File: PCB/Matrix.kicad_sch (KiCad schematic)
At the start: 133 parts, among them SW1 MX, SW10 MX, SW11 MX, SW12 MX, SW13 MX, SW14 MX, SW15 MX, SW16 MX, SW17 MX, SW18 MX, SW19 MX, SW2 MX, SW20 MX, SW21 MX, SW22 MX, SW23 MX, SW24 MX, SW25 MX, SW26 MX, SW27 MX, SW28 MX, SW29 MX, SW3 MX, SW30 MX, SW31 MX, SW32 MX, SW33 MX, SW34 MX, SW35 MX, SW36 MX, SW37 MX, SW38 MX, SW39 MX, SW4 MX, SW40 MX, SW41 MX, SW42 MX, SW43 MX, SW44 MX, SW45 MX, SW46 MX, SW47 MX, SW48 MX, SW49 MX, SW5 MX, SW50 MX, SW51 MX, SW52 MX, SW53 MX, SW54 MX, SW55 MX, SW56 MX, SW57 MX, SW58 MX, SW59 MX, SW6 MX, SW60 MX, SW61 MX, SW62 MX, SW63 MX, SW64 Encoder, SW7 MX, SW8 MX, SW9 MX

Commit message: Massive mistake corrections and clarifications.
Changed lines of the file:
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@@
-    (stroke (width 0) (type default))
-  )
-  (wire (pts (xy 259.08 74.93) (xy 261.62 74.93))
     (stroke (width 0) (type default))
   )
@@
     (stroke (width 0) (type default))
   )
-  (wire (pts (xy 259.08 74.93) (xy 259.08 72.39))
+  (wire (pts (xy 259.08 72.39) (xy 259.08 74.93))
     (stroke (width 0) (type default))
   )
@@
     (stroke (width 0) (type default))
   )
-  (wire (pts (xy 251.46 52.07) (xy 251.46 67.31))
-    (stroke (width 0) (type default))
-  )
   (wire (pts (xy 87.63 88.9) (xy 87.63 86.36))
     (stroke (width 0) (type default))
@@
     (stroke (width 0) (type default))
   )
+  (wire (pts (xy 248.92 52.07) (xy 248.92 54.61))
+    (stroke (width 0) (type default))
+  )
   (wire (pts (xy 133.35 40.64) (xy 133.35 55.88))
     (stroke (width 0) (type default))
@@
     (stroke (width 0) (type default))
   )
+  (wire (pts (xy 256.54 49.53) (xy 256.54 52.07))
+    (stroke (width 0) (type default))
+  )
   (wire (pts (xy 158.75 71.12) (xy 158.75 86.36))
     (stroke (width 0) (type default))
@@
     (stroke (width 0) (type default))
   )
-  (wire (pts (xy 248.92 52.07) (xy 251.46 52.07))
-    (stroke (width 0) (type default))
-  )
   (wire (pts (xy 52.07 55.88) (xy 52.07 71.12))
     (stroke (width 0) (type default))
@@
     (stroke (width 0) (type default))
   )
+  (wire (pts (xy 251.46 67.31) (xy 251.46 49.53))
+    (stroke (width 0) (type default))
+  )
   (wire (pts (xy 54.61 71.12) (xy 52.07 71.12))
     (stroke (width 0) (type default))
@@
     (stroke (width 0) (type default))
   )
+  (wire (pts (xy 251.46 49.53) (xy 256.54 49.53))
+    (stroke (width 0) (type default))
+  )
   (wire (pts (xy 123.19 40.64) (xy 123.19 43.18))
     (stroke (width 0) (type default))
@@
     (stroke (width 0) (type default))
   )
-  (wire (pts (xy 243.84 74.93) (xy 241.3 74.93))
-    (stroke (width 0) (type default))
-  )
   (wire (pts (xy 110.49 43.18) (xy 110.49 40.64))
     (stroke (width 0) (type default))
@@
     (stroke (width 0) (type default))
   )
-  (wire (pts (xy 248.92 54.61) (xy 246.38 54.61))
-    (stroke (width 0) (type default))
-  )
   (wire (pts (xy 87.63 86.36) (xy 85.09 86.36))
     (stroke (width 0) (type default))
@@
   (wire (pts (xy 215.9 86.36) (xy 213.36 86.36))
     (stroke (width 0) (type default))
-  )
-  (image (at 205.74 173.99) (scale 1.29633)
-    (data
-      iVBORw0KGgoAAAANSUhEUgAAAgAAAACACAYAAAB9V9ELAAAABHNCSVQICAgIfAhkiAAABRFJREFU
-      eJzt3Uty3DgQBUDZMfe/smdpDz0hCsKvgJe5tdxkg6RUgVcAPz4AAAAAAAAAgBv82H0ClPer8efd
-      UwAH+Ln7BACA9RQAABBIAQAAgeS1PD0z/7d75K1HwD0GUJAZAAAIpAAAgEAKAAAI9M/uE2C51nX9
-      b54Z/+jPB37Tc8MwZgAAIJACAAACKQAAIJAegPv1Zoat+wIA47T21Hhe+TIzAAAQSAEAAIEUAAAQ
-      SA/AfawThnPZR4NlzAAAQCAFAAAEUgAAQCA9AOdpzQhl/nAP795gGDMAABBIAQAAgRQAABBID0B9
-      1vUDMJwZAAAIpAAAgEAKAAAIpAegntGZf+v7wa0rBghgBgAAAikAACCQAgAAAukB2G925v/272+f
-      f/s+A/ZZACKZAQCAQAoAAAikAACAQHoA5mtdV9+bOa9+X7h9AwAOZAYAAAIpAAAgkAIAAALpARiv
-      2rpy69g/Z3yASGYAACCQAgAAAikAACCQHoB+1TL/VqPX8Vf/vgB8mAEAgEgKAAAIpAAAgEB6AN6t
-      3su/9fijj7c6w9/dQ7H7+NDCuzcYxgwAAARSAABAIAUAAATSA/C33Znw7Iyv9/N3Z5C7jz9a7/c5
-      vedk9/Htg9Hm9vuj9/OrPc+fMgMAAIEUAAAQSAEAAIFuz6u+Ynem9bQ642r9vNHnVz3Tn50pjrZ6
-      /HePT/X77bTr8bT7fG6/P1oNvb5mAAAgkAIAAAIpAAAgUGIPwOwMu9qYzl7XelrG13r8ahnu6HdT
-      rF4Hf9rxVl+P1Z/fe7xWq++Pascfret6mwEAgEAKAAAIpAAAgEA3vgugWia32u69rGc7rcfiTev3
-      ef58tetV7Xxa3XY93qzuKdndkzG7Z+uovydmAAAgkAIAAAIpAAAg0A09ANX38q/+fuzTMsvTVeth
-      SFd93fxuvT0RT7N/X6/uyRh9vk9TexrMAABAIAUAAARSAABAoBN7AHZn/rvX/d6Wod3utsx/9P0x
-      +vNm369pz8PonqbdPVH8wQwAAARSAABAIAUAAAQ6oQegNfNevQ5/d6bVu/d09Yy62vnt7kGppjXD
-      rz4+ozPk2XvDr+75qfb7Y/d4zTa1J8sMAAAEUgAAQCAFAAAEqtADMDvDqZZZvZmd+dMmffyuyjz/
-      x+z305/mtn1Abrs+Q5kBAIBACgAACKQAAIBAO3oATl8n3Gv2908f391m95ycnsmeLu16vvUErO6x
-      qj5eRzEDAACBFAAAEEgBAACBVvQApGXSq/c1GP35b/9/dwbI54x/n9PGr9rzN/p8ZP5tmsbfDAAA
-      BFIAAEAgBQAABBrRA1At46+2DnV1BrY7AzzN7L3PezNRGehcq5+X6tdz9/2/+/hRzAAAQCAFAAAE
-      UgAAQKDv9AC0ZjSnZTC7M/dqPRWt3q539Qx0ttXvt69+v/TqHc/Rz9vo69v6/FR//nqP39tDsPv7
-      l2IGAAACKQAAIJACAAACfSXf6s3ITs9cdu8rUD3DnX19q6/Tdv//V/VMvZrq47F7L//Tjz9b1/Nm
-      BgAAAikAACCQAgAAAq3oAUi3e1+B1W7L3Kpn2qPXec/OXKu9G+P0Hpbd17vV7r8nu48/mh4AAKCN
-      AgAAAikAACDQd/KOtEz76bTMDQD+YgYAAAIpAAAgkAIAAAKNyKNPz8Rnr8sGgHLMAABAIAUAAARS
-      AABAoBV59env85bpA3AdMwAAEEgBAACBFAAAAAAAAAAAAABwqH8BSZ/NA/X8f8AAAAAASUVORK5C
-      YII=
-    )
   )
   (hierarchical_label "COL6" (shape input) (at 120.65 22.86 90) (fields_autoplaced)
@@
     (effects (font (size 1.27 1.27)) (justify left))
   )
-  (hierarchical_label "GND" (shape output) (at 261.62 74.93 0) (fields_autoplaced)
-    (effects (font (size 1.27 1.27)) (justify left))
-  )
   (hierarchical_label "COL2" (shape input) (at 52.07 22.86 90) (fields_autoplaced)
     (effects (font (size 1.27 1.27)) (justify left))
   )
-  (hierarchical_label "GND" (shape output) (at 241.3 74.93 180) (fields_autoplaced)
-    (effects (font (size 1.27 1.27)) (justify right))
-  )
   (hierarchical_label "COL9" (shape input) (at 158.75 22.86 90) (fields_autoplaced)
     (effects (font (size 1.27 1.27)) (justify left))
   )
-  (hierarchical_label "GND" (shape output) (at 248.92 52.07 180) (fields_autoplaced)
-    (effects (font (size 1.27 1.27)) (justify right))
-  )
   (hierarchical_label "ROW0" (shape output) (at 186.69 35.56 0) (fields_autoplaced)
     (effects (font (size 1.27 1.27)) (justify left))
@@
   (hierarchical_label "COL5" (shape input) (at 90.17 22.86 90) (fields_autoplaced)
     (effects (font (size 1.27 1.27)) (justify left))
-  )
-  (hierarchical_label "+3V3" (shape input) (at 246.38 54.61 180) (fields_autoplaced)
-    (effects (font (size 1.27 1.27)) (justify right))
   )
   (hierarchical_label "ROW2" (shape output) (at 203.2 66.04 180) (fields_autoplaced)
@@
     )
   )
+  (symbol (lib_id "power:+3V3") (at 248.92 52.07 0) (unit 1)
+    (in_bom yes) (on_board yes) (dnp no)
+    (property "Reference" "#PWR07" (at 248.92 55.88 0)
+      (effects (font (size 1.27 1.27)) hide)
+    )
+    (property "Value" "+3V3" (at 245.11 50.8 0)
+      (effects (font (size 1.27 1.27)))
+    )
+    (property "Footprint" "" (at 248.92 52.07 0)
+      (effects (font (size 1.27 1.27)) hide)
+    )
+    (property "Datasheet" "" (at 248.92 52.07 0)
+      (effects (font (size 1.27 1.27)) hide)
+    )
+    (pin "1")
+    (instances
+      (project "Honeydew"
+        (path "/534caec7-cf60-4f90-b1ed-42c9d445ef0f/c1819a82-630d-421e-8b73-d65ee471609e"
+          (reference "#PWR07") (unit 1)
+        )
+      )
+    )
+  )
   (symbol (lib_id "Device:R_Small") (at 264.16 64.77 90) (mirror x) (unit 1)
     (in_bom yes) (on_board yes) (dnp no)
@@
     )
   )
+  (symbol (lib_id "power:GND") (at 259.08 74.93 0) (unit 1)
+    (in_bom yes) (on_board yes) (dnp no)
+    (property "Reference" "#PWR026" (at 259.08 81.28 0)
+      (effects (font (size 1.27 1.27)) hide)
+    )
+    (property "Value" "GND" (at 259.08 78.74 0)
+      (effects (font (size 1.27 1.27)))
+    )
+    (property "Footprint" "" (at 259.08 74.93 0)
+      (effects (font (size 1.27 1.27)) hide)
+    )
+    (property "Datasheet" "" (at 259.08 74.93 0)
+      (effects (font (size 1.27 1.27)) hide)
+    )
+    (pin "1")
+    (instances
+      (project "Honeydew"
+        (path "/534caec7-cf60-4f90-b1ed-42c9d445ef0f/c1819a82-630d-421e-8b73-d65ee471609e"
+          (reference "#PWR026") (unit 1)
+        )
+      )
+    )
+  )
   (symbol (lib_id "Cantaloupe:SW_SPST_Small") (at 44.45 55.88 0) (mirror y) (unit 1)
     (in_bom no) (on_board yes) (dnp no)
@@
     )
   )
+  (symbol (lib_id "power:GND") (at 243.84 74.93 0) (unit 1)
+    (in_bom yes) (on_board yes) (dnp no)
+    (property "Reference" "#PWR021" (at 243.84 81.28 0)
+      (effects (font (size 1.27 1.27)) hide)
+    )
+    (property "Value" "GND" (at 243.84 78.74 0)
+      (effects (font (size 1.27 1.27)))
+    )
+    (property "Footprint" "" (at 243.84 74.93 0)
+      (effects (font (size 1.27 1.27)) hide)
+    )
+    (property "Datasheet" "" (at 243.84 74.93 0)
+      (effects (font (size 1.27 1.27)) hide)
+    )
+    (pin "1")
+    (instances
+      (project "Honeydew"
+        (path "/534caec7-cf60-4f90-b1ed-42c9d445ef0f/c1819a82-630d-421e-8b73-d65ee471609e"
+          (reference "#PWR021") (unit 1)
+        )
+      )
+    )
+  )
   (symbol (lib_id "Device:D_Small") (at 148.59 60.96 270) (mirror x) (unit 1)
     (in_bom yes) (on_board yes) (dnp no)
@@
         )
       )
+    )
+  )
+  (symbol (lib_id "power:GND") (at 256.54 52.07 0) (unit 1)
+    (in_bom yes) (on_board yes) (dnp no)
+    (property "Reference" "#PWR027" (at 256.54 58.42 0)
+      (effects (font (size 1.27 1.27)) hide)
+    )
+    (property "Value" "GND" (at 260.35 53.34 0)
+      (effects (font (size 1.27 1.27)))
+    )
+    (property "Footprint" "" (at 256.54 52.07 0)
+      (effects (font (size 1.27 1.27)) hide)
+    )
+    (property "Datasheet" "" (at 256.54 52.07 0)
+      (effects (font (size 1.27 1.27)) hide)
+    )
+    (pin "1")
+    (instances
+      (project "Honeydew"
+        (path "/534caec7-cf60-4f90-b1ed-42c9d445ef0f/c1819a82-630d-421e-8b73-d65ee471609e"
+          (reference "#PWR027") (unit 1)
+        )
+      )

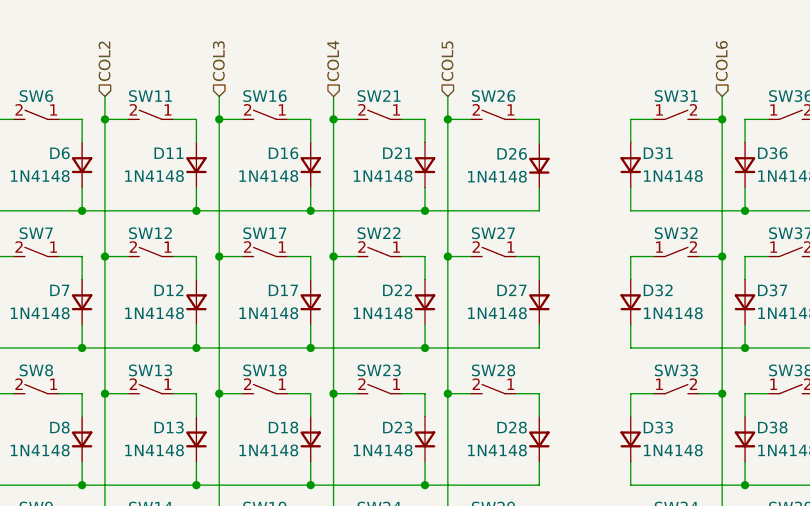
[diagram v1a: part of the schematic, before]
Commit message: Rewording of readme. Added files for JLC PCBA. Changed USB C connector and moved it away from board.
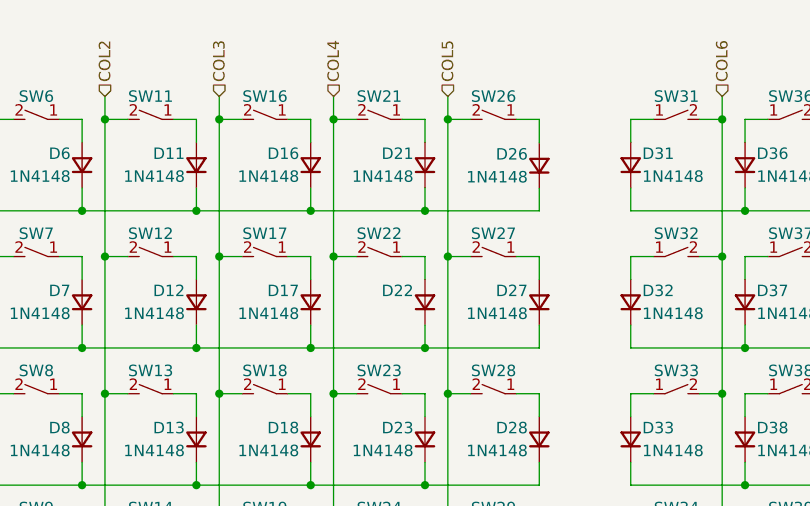
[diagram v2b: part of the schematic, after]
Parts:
- C1, C2: LCSC (none) -> C15195; LCSC part number C15195 -> (none)
- D1, D10, D11, D12, D13, D14, D15, D16, D17, D18, D19, D2, D20, D21, D22, D23, D24, D25, D26, D27, D28, D29, D3, D30, D31, D32, D33, D34, D35, D36, D37, D38, D39, D4, D40, D41, D42, D43, D44, D45, D46, D47, D48, D49, D5, D50, D51, D52, D53, D54, D55, D56, D57, D58, D59, D6, D60, D61, D62, D63, D7, D8, D9: LCSC (none) -> C81598; LCSC part number C81598 -> (none)
- R1, R2, R3, R4: LCSC (none) -> C25744; LCSC part number C25744 -> (none)
- SW1, SW10, SW11, SW12, SW13, SW14, SW15, SW16, SW17, SW18, SW19, SW2, SW20, SW21, SW22, SW23, SW24, SW25, SW26, SW27, SW28, SW29, SW3, SW30, SW31, SW32, SW33, SW34, SW35, SW36, SW37, SW38, SW39, SW4, SW40, SW41, SW42, SW43, SW44, SW45, SW46, SW47, SW48, SW49, SW5, SW50, SW51, SW52, SW53, SW54, SW55, SW56, SW57, SW58, SW59, SW6, SW60, SW61, SW62, SW63, SW7, SW8, SW9: LCSC (none) -> C5156480; now in the parts list
- SW64: LCSC (none) -> C470483

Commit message: Shifted MCU up to reduce length of USB traces. Added holes for JLC assembly.
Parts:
- SW1, SW10, SW11, SW12, SW13, SW14, SW15, SW16, SW17, SW18, SW19, SW2, SW20, SW21, SW22, SW23, SW24, SW25, SW26, SW27, SW28, SW29, SW3, SW30, SW31, SW32, SW33, SW34, SW35, SW36, SW37, SW38, SW39, SW4, SW40, SW41, SW42, SW43, SW44, SW45, SW46, SW47, SW48, SW49, SW5, SW50, SW51, SW52, SW53, SW54, SW55, SW56, SW57, SW58, SW59, SW6, SW60, SW61, SW62, SW63, SW7, SW8, SW9: value MX -> CPG151101S11; LCSC C5156480 -> C5184526

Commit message: More V1.1 updates
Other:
- moved on the sheet: C1, C2, R1, R2, R3, R4, SW64

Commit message: Initial V2.0 update.
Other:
- moved on the sheet: C1, C2, R1, R2, R3, R4, SW64

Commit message: Additional changes.
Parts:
- D1, D10, D11, D12, D13, D14, D15, D16, D17, D18, D19, D2, D20, D21, D22, D23, D24, D25, D26, D27, D28, D29, D3, D30, D31, D32, D33, D34, D35, D36, D37, D38, D39, D4, D40, D41, D42, D43, D44, D45, D46, D47, D48, D49, D5, D50, D51, D52, D53, D54, D55, D56, D57, D58, D59, D6, D60, D61, D62, D63, D7, D8, D9: footprint Honeydew:D_SOD-123 -> Honeydew:D_SOD-323; LCSC C81598 -> SOD-323

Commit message: Large update.
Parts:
- C1, C2: Voltage (none) -> 50V
- D1, D10, D11, D12, D13, D14, D15, D16, D17, D18, D19, D2, D20, D21, D22, D23, D24, D25, D26, D27, D28, D29, D3, D30, D31, D32, D33, D34, D35, D36, D37, D38, D39, D4, D40, D41, D42, D43, D44, D45, D46, D47, D48, D49, D5, D50, D51, D52, D53, D54, D55, D56, D57, D58, D59, D6, D60, D61, D62, D63, D7, D8, D9: LCSC SOD-323 -> C2128
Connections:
- net COL12 renamed COLM
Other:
- moved on the sheet: D31, D32, D33, D34, D35, D36, D37, D38, D39, D40, D41, D42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
